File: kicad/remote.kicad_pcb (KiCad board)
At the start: 2 copper layers, 42 parts, among them J1 Conn_01x03, SW1 SW_SPDT_MSM, SW2 SW_SPDT_MSM, SW3 SW_SPDT_MSM, SW4 SW_SPDT_MSM, SW5 SW_Push, SW6 SW_Push, SW7 SW_Push, SW8 SW_Push, U1 74LS165, U2 74LS165, U3 Arduino_Nano_v3.x, U4 AP1117, U5 nRF24L01+, U6 OLED_7pin_4SPI, U7 COM-09032, U8 COM-09032

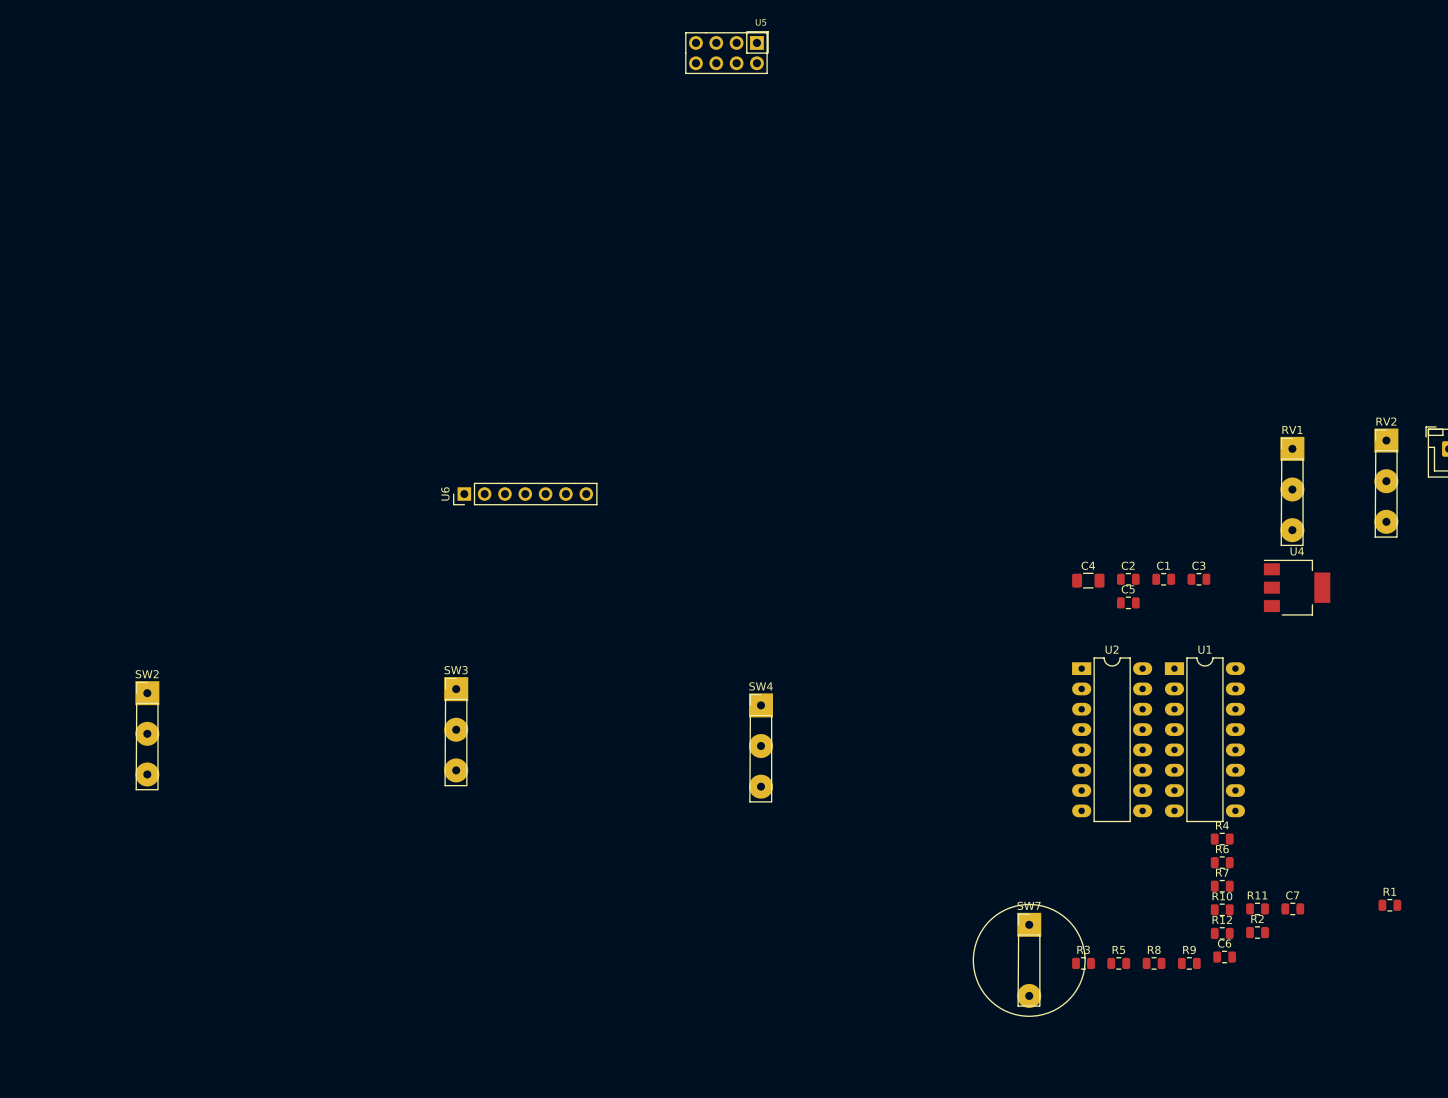
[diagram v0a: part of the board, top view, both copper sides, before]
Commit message: Add more switches, footprints.
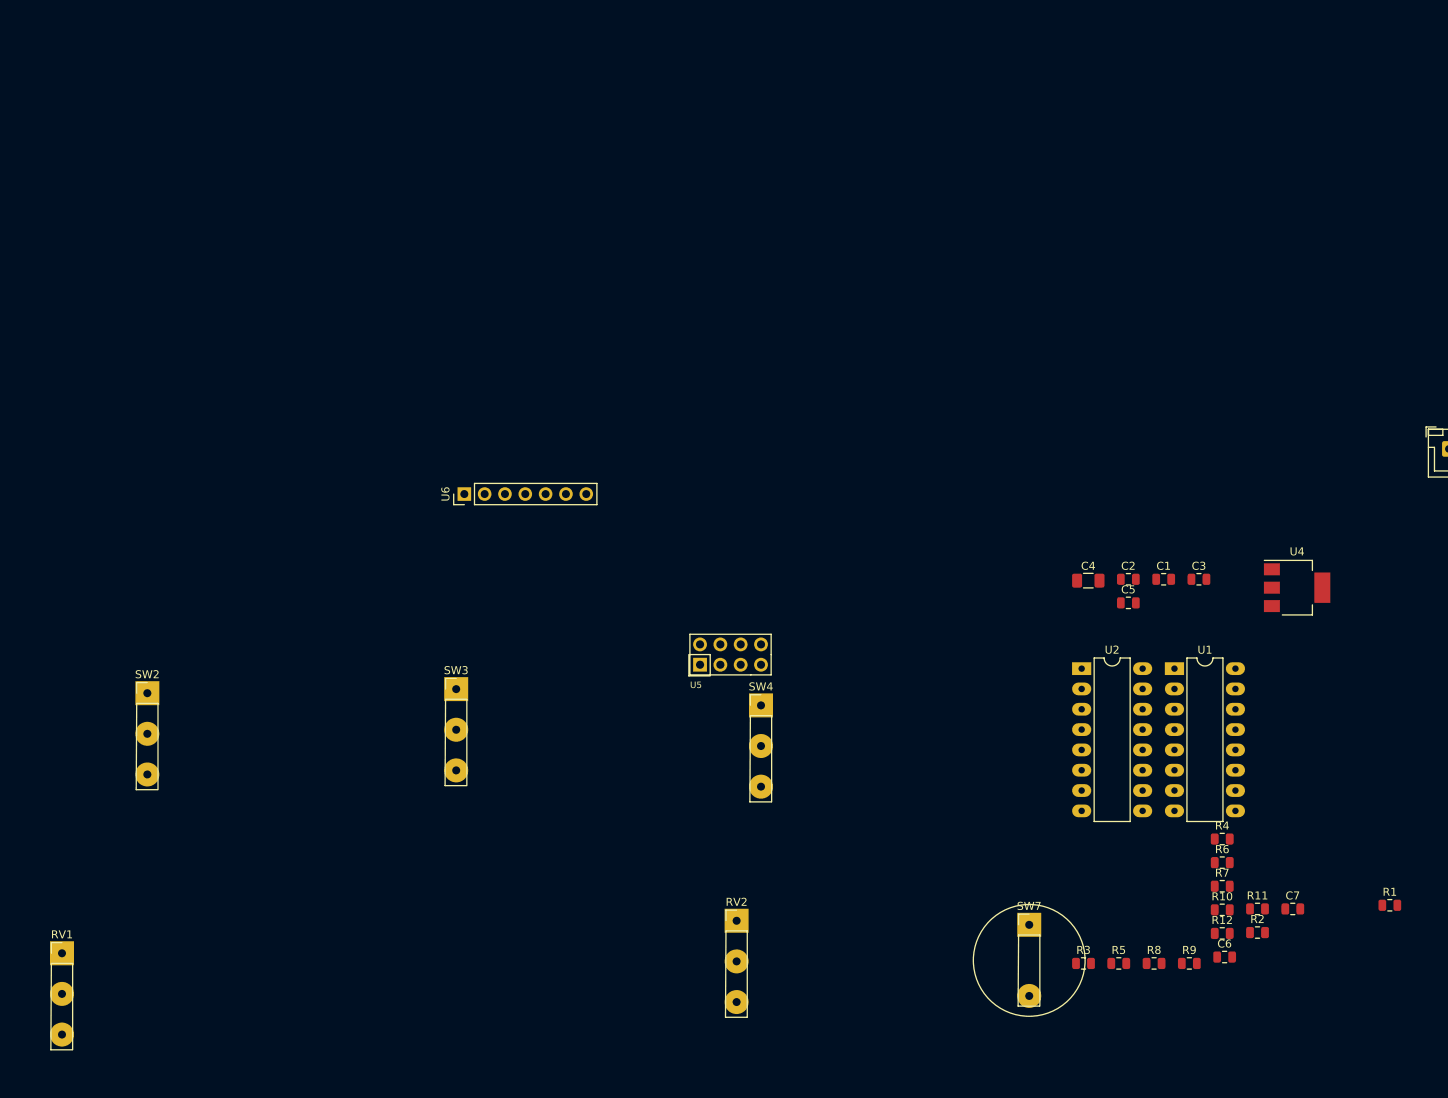
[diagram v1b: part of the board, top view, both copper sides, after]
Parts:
- moved RV1 166.2 mm to (65.0, 87.4)
- moved RV2 101.0 mm to (149.4, 83.3)
- moved U5 81.4 mm to (143.3, 52.8), turned to 180 degrees
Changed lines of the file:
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@@
     (solder_mask_min_width 0.25)
     (aux_axis_origin 0 0)
-    (visible_elements FFFFFF7F)
+    (visible_elements FFFFF77F)
     (pcbplotparams
       (layerselection 0x010fc_ffffffff)
@@
   )
   (module Remote:Switch_1x03_P5.08mm (layer F.Cu)
-    (at 218.823001 24.325001)
+    (at 65.024 87.376)
     (descr "Through hole straight pin header, 1x03, 2.54mm pitch, single row")
     (tags "Through hole pin header THT 1x03 2.54mm single row")
@@
   )
   (module Remote:Switch_1x03_P5.08mm (layer F.Cu)
-    (at 230.573001 23.285001)
+    (at 149.352 83.312)
     (descr "Through hole straight pin header, 1x03, 2.54mm pitch, single row")
     (tags "Through hole pin header THT 1x03 2.54mm single row")
@@
       (scale (xyz 1 1 1))
       (rotate (xyz 0 0 0))
-    )
-  )
-  (module Remote:nRF24L01 (layer F.Cu)
-    (at 153.416 -27.94)
-    (descr NRF24L01)
-    (tags "nRF 24 NRF24L01 NRF24L01+")
-    (fp_text reference U5 (at -1.016 -1.016) (layer F.SilkS)
-      (effects (font (size 0.8 0.8) (thickness 0.16)))
-    )
-    (fp_text value nRF24L01+ (at -8.382 7.112) (layer F.Fab) hide
-      (effects (font (size 0.8 0.8) (thickness 0.16)))
-    )
-    (fp_line (start -2.794 0.127) (end -0.127 0.127) (layer F.SilkS) (width 0.15))
-    (fp_line (start -0.127 0.127) (end -0.127 2.794) (layer F.SilkS) (width 0.15))
-    (fp_line (start 2.54 0) (end -12.71 0) (layer B.CrtYd) (width 0.15))
-    (fp_line (start -12.71 0) (end -12.71 28.8) (layer B.CrtYd) (width 0.15))
-    (fp_line (start -12.71 28.8) (end 2.54 28.8) (layer B.CrtYd) (width 0.15))
-    (fp_line (start 2.54 28.8) (end 2.54 0) (layer B.CrtYd) (width 0.15))
-    (fp_line (start -7.874 0.254) (end -10.414 0.254) (layer F.SilkS) (width 0.15))
-    (fp_line (start -10.414 0.254) (end -10.414 2.794) (layer F.SilkS) (width 0.15))
-    (fp_line (start -2.794 0.254) (end -2.794 2.794) (layer F.SilkS) (width 0.15))
-    (fp_line (start -2.794 2.794) (end -0.254 2.794) (layer F.SilkS) (width 0.15))
-    (fp_line (start -10.894 -0.226) (end -10.894 5.824) (layer F.CrtYd) (width 0.05))
-    (fp_line (start 0.256 -0.226) (end 0.256 5.824) (layer F.CrtYd) (width 0.05))
-    (fp_line (start -10.894 -0.226) (end 0.256 -0.226) (layer F.CrtYd) (width 0.05))
-    (fp_line (start -10.894 5.824) (end 0.256 5.824) (layer F.CrtYd) (width 0.05))
-    (fp_line (start -7.874 0.254) (end -0.254 0.254) (layer F.SilkS) (width 0.15))
-    (fp_line (start -0.254 0.254) (end -0.254 5.334) (layer F.SilkS) (width 0.15))
-    (fp_line (start -0.254 5.334) (end -10.414 5.334) (layer F.SilkS) (width 0.15))
-    (fp_line (start -10.414 5.334) (end -10.414 2.794) (layer F.SilkS) (width 0.15))
-    (pad 7 thru_hole oval (at -9.144 1.524) (size 1.7272 1.7272) (drill 1.016) (layers *.Cu *.Mask F.SilkS)
-      (net 48 MISO))
-    (pad 8 thru_hole oval (at -9.144 4.064) (size 1.7272 1.7272) (drill 1.016) (layers *.Cu *.Mask F.SilkS)
-      (net 49 "Net-(U5-Pad8)"))
-    (pad 5 thru_hole oval (at -6.604 1.524) (size 1.7272 1.7272) (drill 1.016) (layers *.Cu *.Mask F.SilkS)
-      (net 42 SCK))
-    (pad 6 thru_hole oval (at -6.604 4.064) (size 1.7272 1.7272) (drill 1.016) (layers *.Cu *.Mask F.SilkS)
-      (net 46 MOSI))
-    (pad 3 thru_hole oval (at -4.064 1.524) (size 1.7272 1.7272) (drill 1.016) (layers *.Cu *.Mask F.SilkS)
-      (net 43 CE))
-    (pad 4 thru_hole oval (at -4.064 4.064) (size 1.7272 1.7272) (drill 1.016) (layers *.Cu *.Mask F.SilkS)
-      (net 44 CSN))
-    (pad 1 thru_hole rect (at -1.524 1.524) (size 1.7272 1.7272) (drill 1.016) (layers *.Cu *.Mask F.SilkS)
-      (net 1 GND))
-    (pad 2 thru_hole oval (at -1.524 4.064) (size 1.7272 1.7272) (drill 1.016) (layers *.Cu *.Mask F.SilkS)
-      (net 3 +3V3))
-    (model Socket_Strips.3dshapes/Socket_Strip_Straight_2x04_Pitch2.54mm.wrl
-      (offset (xyz -5.333999919891357 -2.79399995803833 0))
-      (scale (xyz 1 1 1))
-      (rotate (xyz 0 0 0))
-    )
-    (model Pin_Headers.3dshapes/Pin_Header_Straight_2x04_Pitch2.54mm.wrl
-      (offset (xyz -1.600199975967407 -4.038599939346313 11.22679983139038))
-      (scale (xyz 1 1 1))
-      (rotate (xyz 0 180 90))
-    )
-    (model ${MYSLOCAL}/mysensors.3dshapes/mysensors_radios.3dshapes/nrf24l01.wrl
-      (offset (xyz -7.619999885559082 -14.40179978370666 12.06499981880188))
-      (scale (xyz 0.395 0.395 0.395))
-      (rotate (xyz 0 0 0))
-    )
-    (model Housings_DFN_QFN.3dshapes/QFN-20-1EP_4x4mm_Pitch0.5mm.wrl
-      (offset (xyz -5.58799991607666 -12.95399980545044 12.92859980583191))
-      (scale (xyz 1 1 1))
-      (rotate (xyz 0 0 0))
-    )
-    (model ${MYSLOCAL}/mysensors.3dshapes/w.lain.3dshapes/crystal/crystal_hc-49s.wrl
-      (offset (xyz -12.69999980926514 -12.06499981880188 12.95399980545044))
-      (scale (xyz 1 1 1))
-      (rotate (xyz 0 0 90))
     )
   )
@@
     )
   )
+  (module Remote:nRF24L01 (layer F.Cu)
+    (at 143.256 52.832 180)
+    (descr NRF24L01)
+    (tags "nRF 24 NRF24L01 NRF24L01+")
+    (fp_text reference U5 (at -1.016 -1.016) (layer F.SilkS)
+      (effects (font (size 0.8 0.8) (thickness 0.16)))
+    )
+    (fp_text value nRF24L01+ (at -8.382 7.112) (layer F.Fab) hide
+      (effects (font (size 0.8 0.8) (thickness 0.16)))
+    )
+    (fp_line (start -2.794 0.127) (end -0.127 0.127) (layer F.SilkS) (width 0.15))
+    (fp_line (start -0.127 0.127) (end -0.127 2.794) (layer F.SilkS) (width 0.15))
+    (fp_line (start 2.54 0) (end -12.71 0) (layer B.CrtYd) (width 0.15))
+    (fp_line (start -12.71 0) (end -12.71 40.1828) (layer B.CrtYd) (width 0.15))
+    (fp_line (start -12.71 40.1828) (end 2.54 40.1828) (layer B.CrtYd) (width 0.15))
+    (fp_line (start 2.54 40.1828) (end 2.54 0) (layer B.CrtYd) (width 0.15))
+    (fp_line (start -7.874 0.254) (end -10.414 0.254) (layer F.SilkS) (width 0.15))
+    (fp_line (start -10.414 0.254) (end -10.414 2.794) (layer F.SilkS) (width 0.15))
+    (fp_line (start -2.794 0.254) (end -2.794 2.794) (layer F.SilkS) (width 0.15))
+    (fp_line (start -2.794 2.794) (end -0.254 2.794) (layer F.SilkS) (width 0.15))
+    (fp_line (start -10.894 -0.226) (end -10.894 5.824) (layer F.CrtYd) (width 0.05))
+    (fp_line (start 0.256 -0.226) (end 0.256 5.824) (layer F.CrtYd) (width 0.05))
+    (fp_line (start -10.894 -0.226) (end 0.256 -0.226) (layer F.CrtYd) (width 0.05))
+    (fp_line (start -10.894 5.824) (end 0.256 5.824) (layer F.CrtYd) (width 0.05))
+    (fp_line (start -7.874 0.254) (end -0.254 0.254) (layer F.SilkS) (width 0.15))
+    (fp_line (start -0.254 0.254) (end -0.254 5.334) (layer F.SilkS) (width 0.15))
+    (fp_line (start -0.254 5.334) (end -10.414 5.334) (layer F.SilkS) (width 0.15))
+    (fp_line (start -10.414 5.334) (end -10.414 2.794) (layer F.SilkS) (width 0.15))
+    (pad 7 thru_hole oval (at -9.144 1.524 180) (size 1.7272 1.7272) (drill 1.016) (layers *.Cu *.Mask F.SilkS)
+      (net 48 MISO))
+    (pad 8 thru_hole oval (at -9.144 4.064 180) (size 1.7272 1.7272) (drill 1.016) (layers *.Cu *.Mask F.SilkS)
+      (net 49 "Net-(U5-Pad8)"))
+    (pad 5 thru_hole oval (at -6.604 1.524 180) (size 1.7272 1.7272) (drill 1.016) (layers *.Cu *.Mask F.SilkS)
+      (net 42 SCK))
+    (pad 6 thru_hole oval (at -6.604 4.064 180) (size 1.7272 1.7272) (drill 1.016) (layers *.Cu *.Mask F.SilkS)
+      (net 46 MOSI))
+    (pad 3 thru_hole oval (at -4.064 1.524 180) (size 1.7272 1.7272) (drill 1.016) (layers *.Cu *.Mask F.SilkS)
+      (net 43 CE))
+    (pad 4 thru_hole oval (at -4.064 4.064 180) (size 1.7272 1.7272) (drill 1.016) (layers *.Cu *.Mask F.SilkS)
+      (net 44 CSN))
+    (pad 1 thru_hole rect (at -1.524 1.524 180) (size 1.7272 1.7272) (drill 1.016) (layers *.Cu *.Mask F.SilkS)
+      (net 1 GND))
+    (pad 2 thru_hole oval (at -1.524 4.064 180) (size 1.7272 1.7272) (drill 1.016) (layers *.Cu *.Mask F.SilkS)
+      (net 3 +3V3))
+    (model Socket_Strips.3dshapes/Socket_Strip_Straight_2x04_Pitch2.54mm.wrl
+      (offset (xyz -5.333999919891357 -2.79399995803833 0))
+      (scale (xyz 1 1 1))
+      (rotate (xyz 0 0 0))
+    )
+    (model Pin_Headers.3dshapes/Pin_Header_Straight_2x04_Pitch2.54mm.wrl
+      (offset (xyz -1.600199975967407 -4.038599939346313 11.22679983139038))
+      (scale (xyz 1 1 1))
+      (rotate (xyz 0 180 90))
+    )
+    (model ${MYSLOCAL}/mysensors.3dshapes/mysensors_radios.3dshapes/nrf24l01.wrl
+      (offset (xyz -7.619999885559082 -14.40179978370666 12.06499981880188))
+      (scale (xyz 0.395 0.395 0.395))
+      (rotate (xyz 0 0 0))
+    )
+    (model Housings_DFN_QFN.3dshapes/QFN-20-1EP_4x4mm_Pitch0.5mm.wrl
+      (offset (xyz -5.58799991607666 -12.95399980545044 12.92859980583191))
+      (scale (xyz 1 1 1))
+      (rotate (xyz 0 0 0))
+    )
+    (model ${MYSLOCAL}/mysensors.3dshapes/w.lain.3dshapes/crystal/crystal_hc-49s.wrl
+      (offset (xyz -12.69999980926514 -12.06499981880188 12.95399980545044))
+      (scale (xyz 1 1 1))
+      (rotate (xyz 0 0 90))
+    )
+  )

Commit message: Place switches, etc. Split up into two boards.
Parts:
- added J10: Conn_01x03, Milling:JST_XH_B03B-XH-A_1x03_P2.50mm_Vertical_Milling, F.Cu at (65.8, 191.5)
- added J11: Conn_01x03, Milling:JST_XH_B03B-XH-A_1x03_P2.50mm_Vertical_Milling, F.Cu at (178.1, 194.6)
- added J12: Conn_01x02, Milling:JST_XH_B02B-XH-A_1x02_P2.50mm_Vertical_Milling, F.Cu at (134.4, 227.8)
- added J13: Conn_01x04, Milling:JST_XH_B04B-XH-A_1x04_P2.50mm_Vertical_Milling, F.Cu at (74.4, 154.7)
- added J14: Conn_01x04, Milling:JST_XH_B04B-XH-A_1x04_P2.50mm_Vertical_Milling, F.Cu at (172.0, 155.2)
- added J2: Conn_01x02, Milling:JST_XH_B02B-XH-A_1x02_P2.50mm_Vertical_Milling, F.Cu at (152.4, 201.2)
- added J3: Conn_01x07, Connector_JST:JST_XH_B07B-XH-A_1x07_P2.50mm_Vertical, F.Cu at (284.5, 111.8)
- added J4: Conn_01x03, Milling:JST_XH_B03B-XH-A_1x03_P2.50mm_Vertical_Milling, F.Cu at (78.0, 267.2)
- added J5: Conn_01x03, Milling:JST_XH_B03B-XH-A_1x03_P2.50mm_Vertical_Milling, F.Cu at (114.4, 114.9)
- added J6: Conn_01x02, Milling:JST_XH_B02B-XH-A_1x02_P2.50mm_Vertical_Milling, F.Cu at (73.4, 199.9)
- added J7: Conn_01x03, Milling:JST_XH_B03B-XH-A_1x03_P2.50mm_Vertical_Milling, F.Cu at (77.7, 165.6)
- added J8: Conn_01x08, Connector_JST:JST_XH_B08B-XH-A_1x08_P2.50mm_Vertical, F.Cu at (273.1, 156.2)
- added J9: Conn_01x08, Connector_JST:JST_XH_B08B-XH-A_1x08_P2.50mm_Vertical, F.Cu at (315.0, 156.2)
- added R13: 10k, Resistor_SMD:R_0805_2012Metric, B.Cu at (191.3, 186.9)
- added R14: 10k, Resistor_SMD:R_0805_2012Metric, B.Cu at (197.1, 206.5)
- added R15: 10k, Resistor_SMD:R_0805_2012Metric, B.Cu at (138.1, 223.8)
- added R16: 10k, Resistor_SMD:R_0805_2012Metric, B.Cu at (137.6, 235.2)
- added SW10: SW_Push, Remote:Switch_1x02_P6mm, F.Cu at (210.3, 211.3)
- added SW11: SW_DP3T, Remote:Switch_2x03_P3mm_Slide, F.Cu at (124.5, 229.3)
- added SW9: SW_Push, Remote:Switch_1x02_P6mm, F.Cu at (203.7, 190.5)
- J1: footprint Connector_JST:JST_XH_B03B-XH-A_1x03_P2.50mm_Vertical -> Milling:JST_XH_B03B-XH-A_1x03_P2.50mm_Vertical_Milling
- R1, R10, R11, R12, R2, R3, R4, R5, R6, R7, R8, R9: moved to B.Cu
- RV1, RV2: footprint Remote:Switch_1x03_P5.08mm -> Remote:Potentiometer_4mm_axis
- SW5, SW6, SW7, SW8: footprint Remote:Switch_1x02_P8mm -> Remote:Switch_1x02_P6mm
- U1, U2: footprint Package_DIP:DIP-16_W7.62mm_LongPads -> Milling:DIP-16_W7.62mm_Milling
- moved J1 279.8 mm to (74.9, 251.5)
- moved R11 201.8 mm to (56.4, 207.3)
- moved U5 191.7 mm to (320.0, 127.0)
- moved SW7 188.1 mm to (42.7, 205.7)
- moved U6 187.6 mm to (293.4, 88.9)
- moved R10 179.8 mm to (60.2, 181.4)
- moved R1 173.4 mm to (66.0, 134.9), turned to 180 degrees
- moved R2 160.3 mm to (66.0, 145.3), turned to 180 degrees
- moved R9 158.5 mm to (65.8, 162.6)
- moved R4 153.9 mm to (74.2, 145.3)
- moved C5 144.6 mm to (318.5, 124.0), turned to 90 degrees
- moved C4 143.1 mm to (327.7, 90.2)
- moved U1 133.4 mm to (297.2, 147.3), turned to 90 degrees
- moved C3 129.5 mm to (325.1, 94.0)
- moved R3 127.1 mm to (74.2, 134.6)
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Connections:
- J1 pad 2: A4 -> BAT
- R1 pad 2: Net-(R1-Pad2) -> Net-(J13-Pad1)
- R10 pad 2: Net-(R10-Pad2) -> Net-(J10-Pad2)
- R11 pad 2: Net-(R11-Pad2) -> Net-(J10-Pad3)
- R12 pad 2: Net-(R12-Pad2) -> Net-(J11-Pad1)
- R2 pad 2: Net-(R2-Pad2) -> Net-(J13-Pad2)
- R3 pad 2: Net-(R3-Pad2) -> Net-(J13-Pad3)
- R4 pad 2: Net-(R4-Pad2) -> Net-(J13-Pad4)
- R5 pad 2: Net-(R5-Pad2) -> Net-(J14-Pad1)
- R6 pad 2: Net-(R6-Pad2) -> Net-(J14-Pad2)
- R7 pad 2: Net-(R7-Pad2) -> Net-(J14-Pad3)
- R8 pad 2: Net-(R8-Pad2) -> Net-(J14-Pad4)
- R9 pad 2: Net-(R9-Pad2) -> Net-(J10-Pad1)
- RV1 pad 2: A6 -> A4
- RV2 pad 2: A7 -> A6
- SW1 pad 1: Net-(R1-Pad2) -> Net-(J13-Pad1)
- SW1 pad 3: Net-(R2-Pad2) -> Net-(J13-Pad2)
- SW2 pad 1: Net-(R3-Pad2) -> Net-(J13-Pad3)
- SW2 pad 3: Net-(R4-Pad2) -> Net-(J13-Pad4)
- SW3 pad 1: Net-(R5-Pad2) -> Net-(J14-Pad1)
- SW3 pad 3: Net-(R6-Pad2) -> Net-(J14-Pad2)
- SW4 pad 1: Net-(R7-Pad2) -> Net-(J14-Pad3)
- SW4 pad 3: Net-(R8-Pad2) -> Net-(J14-Pad4)
- SW5 pad 1: Net-(R9-Pad2) -> Net-(J10-Pad1)
- SW6 pad 1: Net-(R10-Pad2) -> Net-(J10-Pad2)
- SW7 pad 1: Net-(R11-Pad2) -> Net-(J10-Pad3)
- SW8 pad 1: Net-(R12-Pad2) -> Net-(J11-Pad1)
- U1 pad 11: Net-(R1-Pad2) -> Net-(J9-Pad1)
- U1 pad 12: Net-(R2-Pad2) -> Net-(J9-Pad2)
- U1 pad 13: Net-(R3-Pad2) -> Net-(J9-Pad3)
- U1 pad 14: Net-(R4-Pad2) -> Net-(J9-Pad4)
- U1 pad 3: Net-(R5-Pad2) -> Net-(J9-Pad8)
- U1 pad 4: Net-(R6-Pad2) -> Net-(J9-Pad7)
- U1 pad 5: Net-(R7-Pad2) -> Net-(J9-Pad6)
- U1 pad 6: Net-(R8-Pad2) -> Net-(J9-Pad5)
- U2 pad 11: Net-(R9-Pad2) -> Net-(J8-Pad1)
- U2 pad 12: Net-(R10-Pad2) -> Net-(J8-Pad2)
- U2 pad 13: Net-(R11-Pad2) -> Net-(J8-Pad3)
- U2 pad 14: Net-(R12-Pad2) -> Net-(J8-Pad4)
- U3 pad 19: Net-(U3-Pad19) -> Net-(J3-Pad1)
- U3 pad 20: Net-(U3-Pad20) -> Net-(J3-Pad2)
- U3 pad 21: Net-(U3-Pad21) -> Net-(J3-Pad3)
- U3 pad 22: Net-(U3-Pad22) -> Net-(J3-Pad4)
- U3 pad 23: A4 -> Net-(J3-Pad5)
- U3 pad 24: PL -> Net-(J3-Pad6)
- U3 pad 25: A6 -> Net-(J3-Pad7)
- U3 pad 26: A7 -> PL
- U7 pad H2: Net-(U3-Pad20) -> Net-(J6-Pad2)
- U7 pad V2: Net-(U3-Pad19) -> Net-(J6-Pad1)
- U8 pad H2: Net-(U3-Pad22) -> Net-(J2-Pad2)
- U8 pad V2: Net-(U3-Pad21) -> Net-(J2-Pad1)
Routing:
- net GND: track 0.00 -> 401.4 mm
- net +5V: track 0.00 -> 81.4 mm
- net Net-(J13-Pad3): track 0.00 -> 4.86 mm
- net Net-(J13-Pad1): track 0.00 -> 4.76 mm
- net Net-(J14-Pad4): track 0.00 -> 4.65 mm
- net Net-(J14-Pad3): track 0.00 -> 4.65 mm
- net Net-(J13-Pad2): track 0.00 -> 4.65 mm
- net Net-(J14-Pad2): track 0.00 -> 4.65 mm
- net Net-(J14-Pad1): track 0.00 -> 4.65 mm
- net Net-(J13-Pad4): track 0.00 -> 4.65 mm
